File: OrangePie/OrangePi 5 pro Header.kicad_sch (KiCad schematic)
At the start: 0 parts

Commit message: Update rest of schematic
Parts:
- added C23, C35: 47uF, Capacitor_SMD:CP_Elec_6.3x5.4, symbol Device:C_Polarized
- added C36, C37, C38, C39: 10uF, PCM_JLCPCB:C_1206, symbol PCM_JLCPCB-Capacitors:1206,10uF
- added J2: Orange pi 5 pro, OrangePi Pro 5:Orange Pi 5 pro, symbol parts_local:Orange pi 5 pro
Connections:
- new net +3V3: J2.32 (3V3), J2.40 (3V3)
- new net +5V: C23.1, C35.1, C36.1, C37.1, C38.1, C39.1, J2.1 (5V), J2.2 (5V)
- new net GND: C23.2, C35.2, C36.2, C37.2, C38.2, C39.2, J2.10 (GND), J2.15 (GND), J2.17 (GND), J2.21 (GND), J2.28 (GND), J2.3 (GND), J2.36 (GND), J2.41 (USB_GND), J2.42 (USB_GND), J2.49 (USB_GND), J2.7 (GND)
- new net GPIO4_B2/PWM14/CAN1_RX: J2.35 (GPIO4_B2/PWM14/CAN1_RX)
- new net GPIO4_B3/PWM15/CAN1_TX: J2.34 (GPIO4_B3/PWM15/CAN1_TX)
- new net USB20_DM3: J2.47 (USB20_DM3)
- new net USB20_DM4: J2.44 (USB20_DM4)
- new net USB20_DP3: J2.48 (USB20_DP3)
- new net USB20_DP4: J2.43 (USB20_DP4)
- no-connect marks 0 -> 28

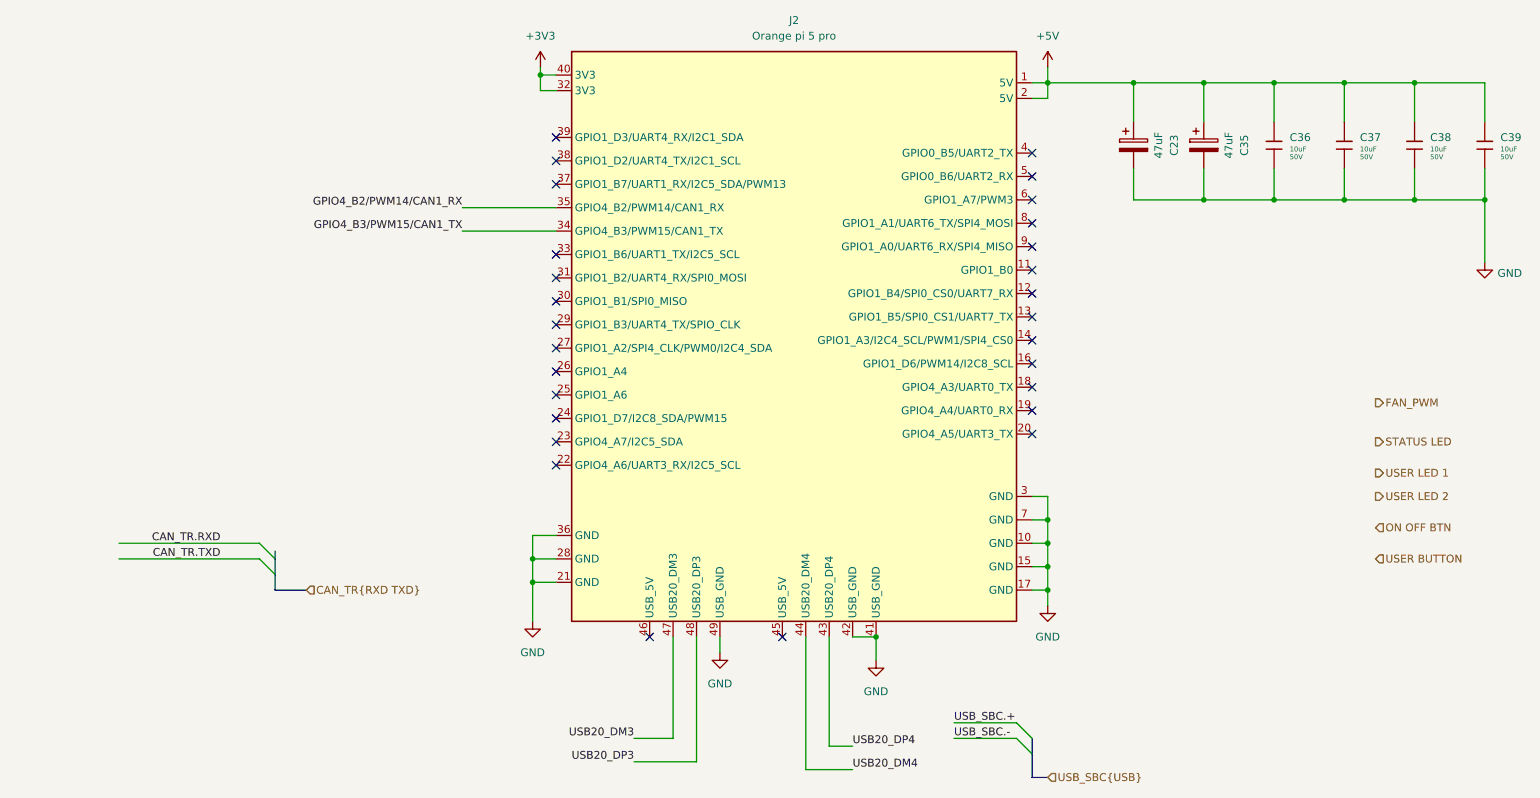
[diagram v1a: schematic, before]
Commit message: Add CH340 debug
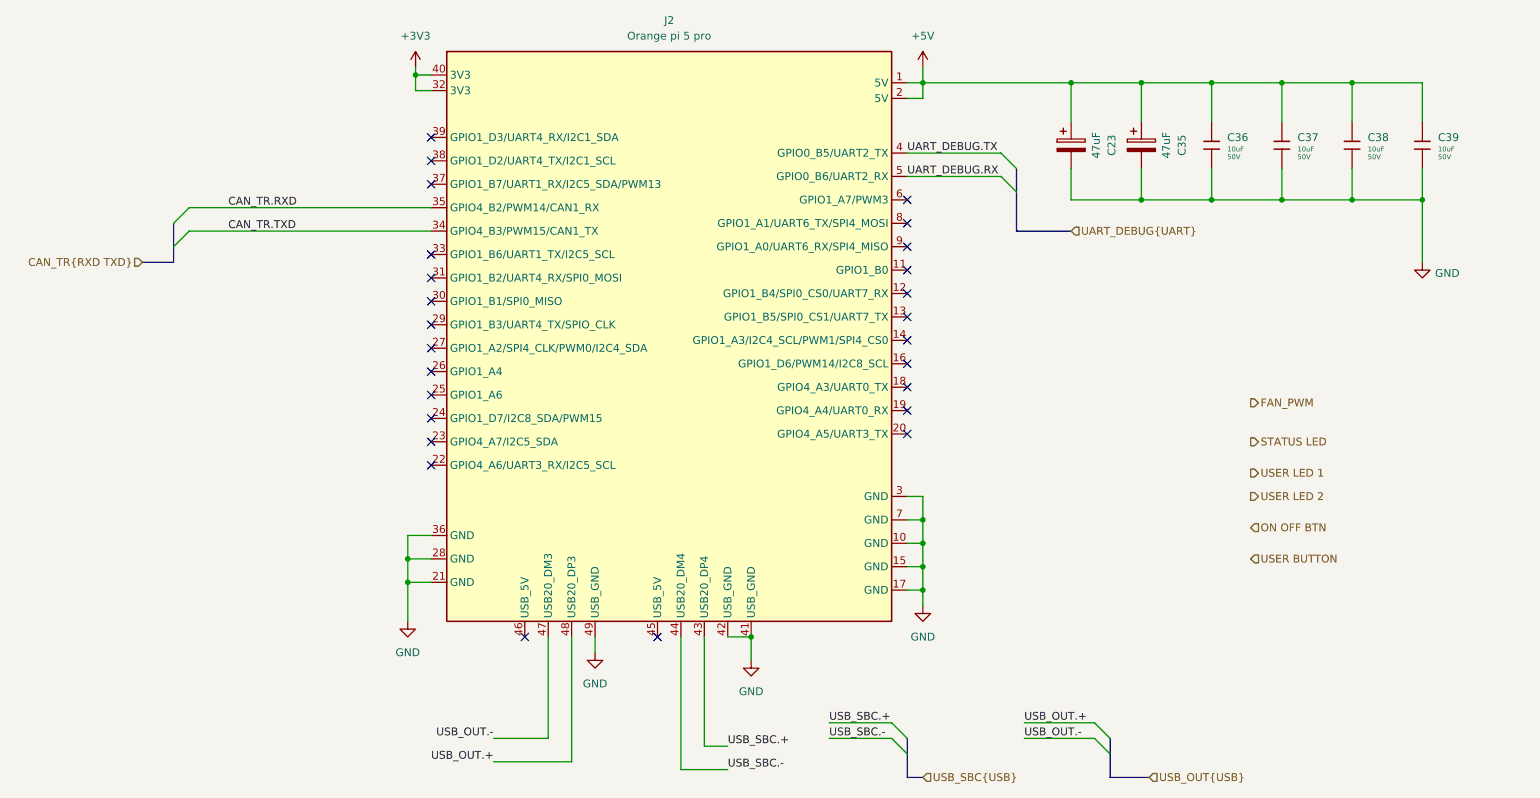
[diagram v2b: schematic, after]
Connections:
- net GPIO4_B2/PWM14/CAN1_RX is gone; now on net CAN_TR.RXD: J2.35 (GPIO4_B2/PWM14/CAN1_RX)
- net GPIO4_B3/PWM15/CAN1_TX is gone; now on net CAN_TR.TXD: J2.34 (GPIO4_B3/PWM15/CAN1_TX)
- net USB20_DM4 is gone; now on net USB_SBC.-: J2.44 (USB20_DM4)
- net USB20_DP4 is gone; now on net USB_SBC.+: J2.43 (USB20_DP4)
- net UART_DEBUG.TX: now reaches J2.4 (GPIO0_B5/UART2_TX)
- net UART_DEBUG.RX: now reaches J2.5 (GPIO0_B6/UART2_RX)
- net USB20_DM3 renamed USB_OUT.-
- net USB20_DP3 renamed USB_OUT.+
- no-connect marks 28 -> 26
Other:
- company: (none) -> ModuCard System
- moved on the sheet: C23, C35, C36, C37, C38, C39, J2
